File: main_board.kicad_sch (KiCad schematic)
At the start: 19 parts, among them SW1 SW_Push, SW2 SW_Push, SW3 SW_Push, U4 QM_XC7A35T_DDR3

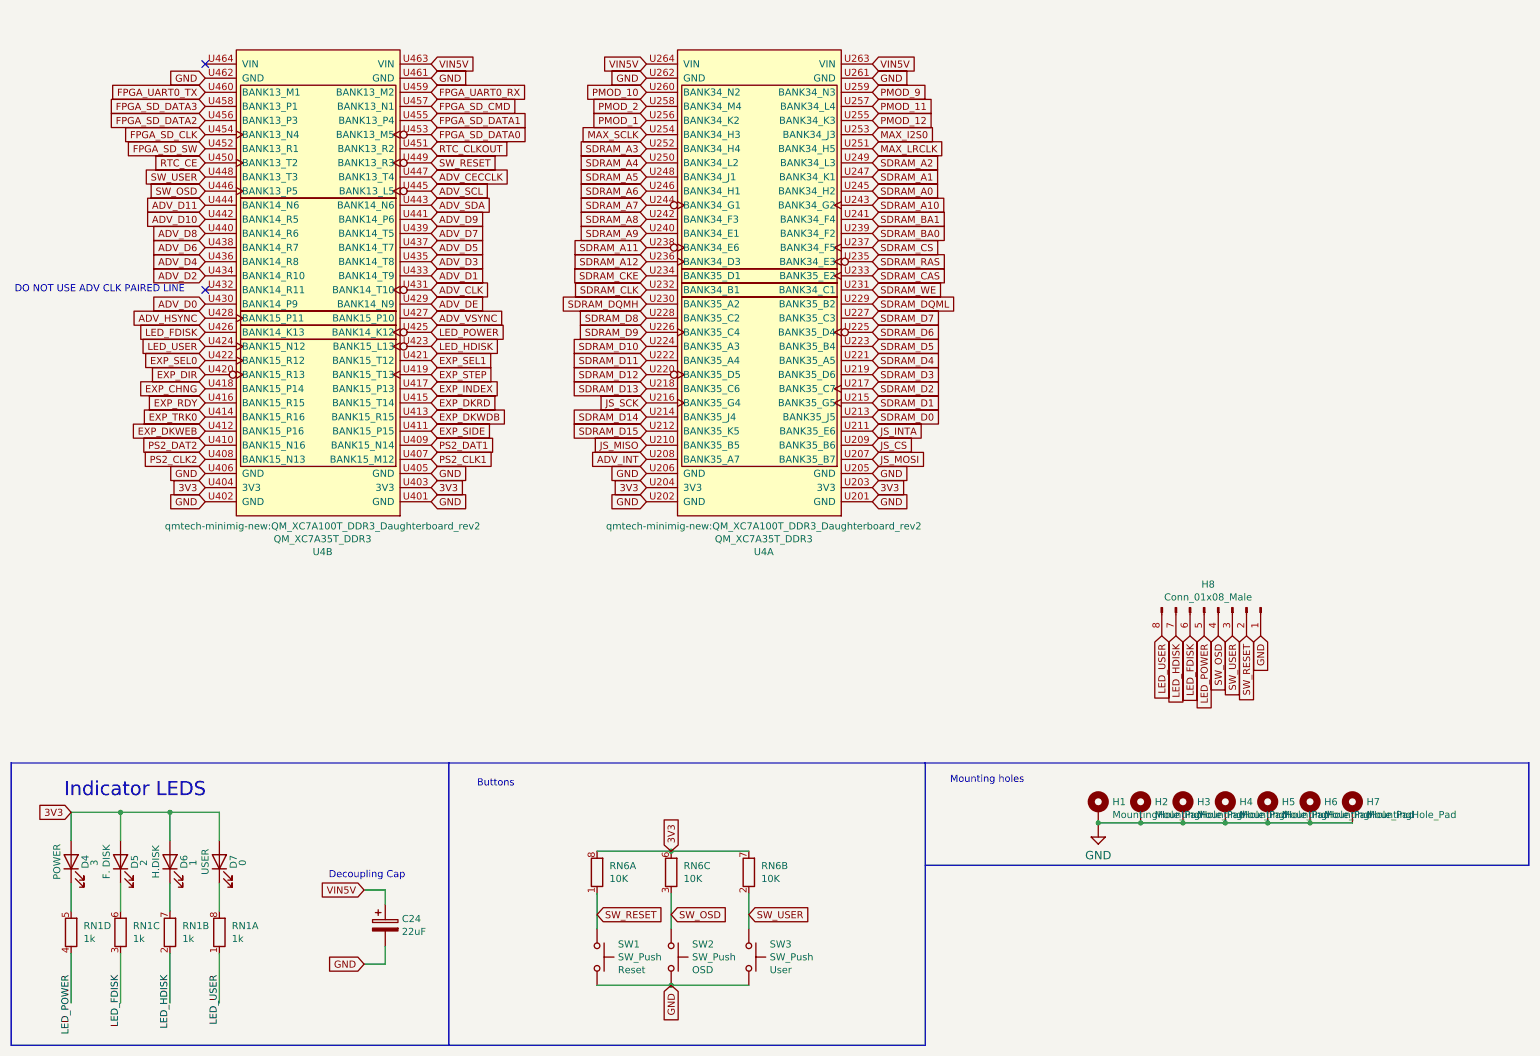
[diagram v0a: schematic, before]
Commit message: Prod version of OpenAARS 5.0 design.
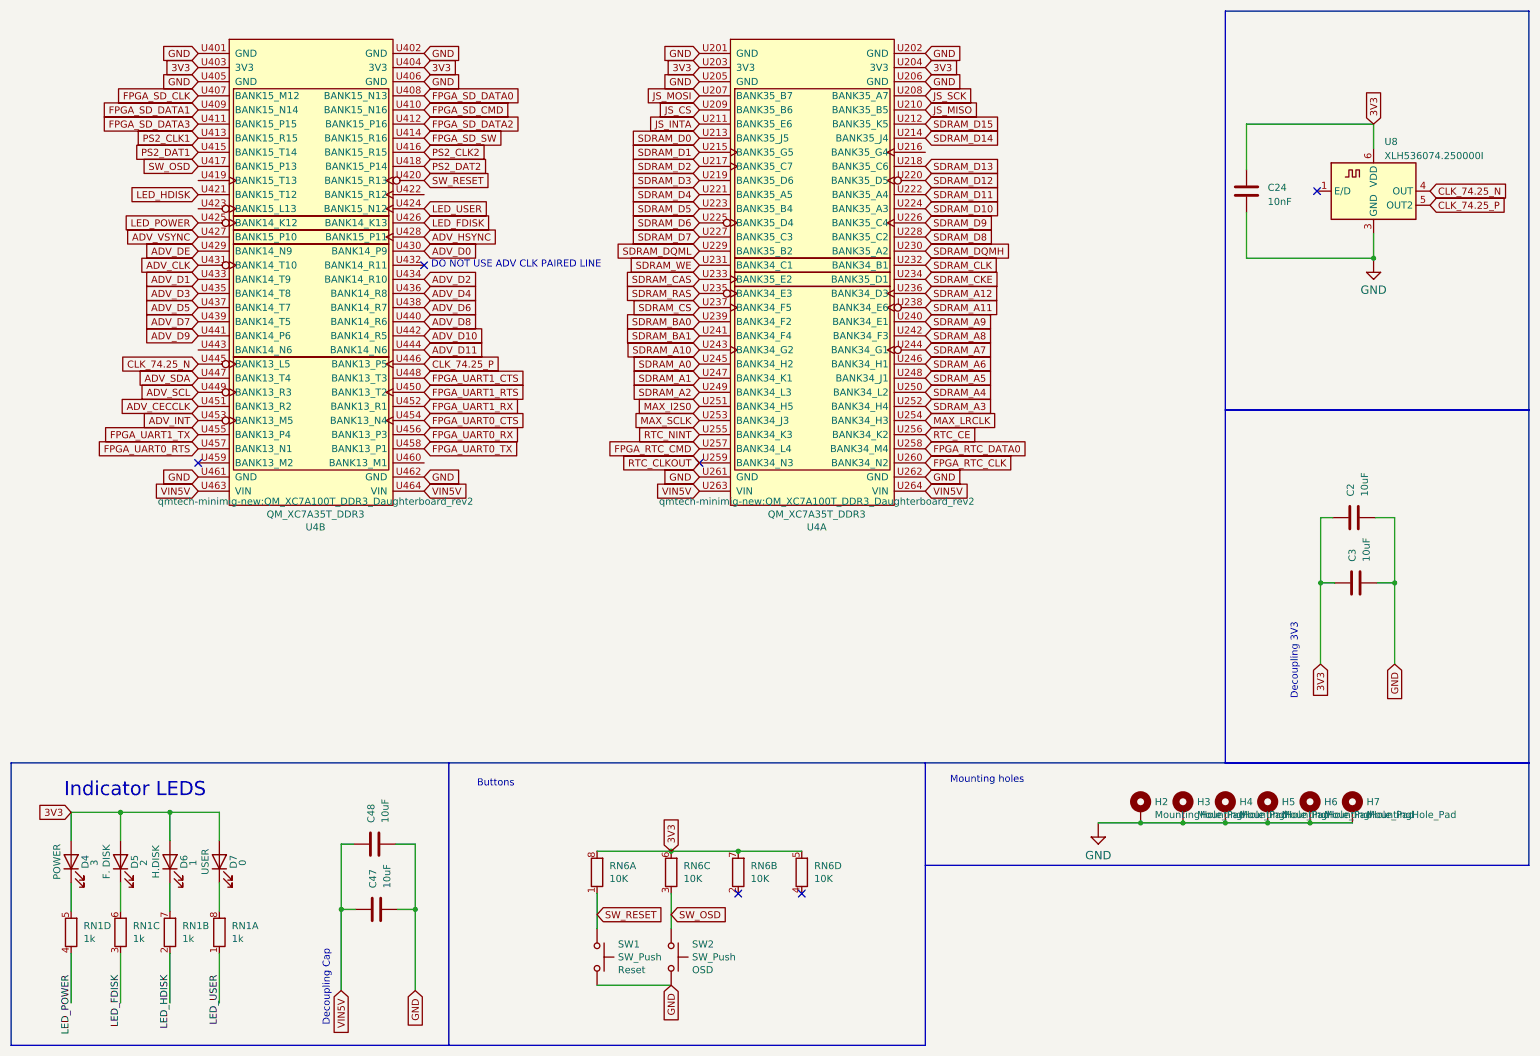
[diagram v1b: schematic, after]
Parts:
- removed C24: 22uF, Capacitor_SMD:CP_Elec_5x5.4, symbol Device:CP
- removed H1: MountingHole_Pad, MountingHole:MountingHole_3.2mm_M3_DIN965_Pad, symbol Mechanical:MountingHole_Pad
- removed H8: Conn_01x08_Male, Connector_PinHeader_2.54mm:PinHeader_1x08_P2.54mm_Vertical, symbol Connector:Conn_01x08_Male
- removed SW3: SW_Push, Button_Switch_SMD:SW_SPST_EVQQ2, symbol Switch:SW_Push
- added C2, C3, C47, C48: 10uF, Capacitor_SMD:C_1206_3216Metric, symbol Device:C
- added C24: 10nF, Capacitor_SMD:C_0603_1608Metric, symbol Device:C
- added unit 4 of RN6
- added U8: XLH536074.250000I, Oscillator:Oscillator_SMD_IDT_JS6-6_5.0x3.2mm_P1.27mm, symbol Oscillator:XUX51
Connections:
- net EXP_CHNG is gone; now on net PS2_DAT2: U4.U418 (BANK15_P14)
- net EXP_DIR is gone; now on net SW_RESET: U4.U420 (BANK15_R13)
- net EXP_DKRD is gone; now on net PS2_DAT1: U4.U415 (BANK15_T14)
- net EXP_DKWDB is gone; now on net PS2_CLK1: U4.U413 (BANK15_R15)
- net EXP_DKWEB is gone; now on net FPGA_SD_DATA2: U4.U412 (BANK15_P16)
- net EXP_INDEX is gone; now on net SW_OSD: U4.U417 (BANK15_P13)
- net EXP_RDY is gone; now on net PS2_CLK2: U4.U416 (BANK15_R15)
- net EXP_SEL1 is gone; now on net LED_HDISK: U4.U421 (BANK15_T12)
- net EXP_SIDE is gone; now on net FPGA_SD_DATA3: U4.U411 (BANK15_P15)
- net EXP_TRK0 is gone; now on net FPGA_SD_SW: U4.U414 (BANK15_R16)
- net PMOD_1 is gone; now on net RTC_CE: U4.U256 (BANK34_K2)
- net PMOD_9 is gone; now on net RTC_CLKOUT: U4.U259 (BANK34_N3)
- net 3V3: now also C2.1, C24.1, C3.1, RN6.5 (R4.2), U8.6 (VDD)
- net ADV_CECCLK: now also U4.U451 (BANK13_R2); no longer U4.U447 (BANK13_T4)
- net ADV_INT: now also U4.U453 (BANK13_M5); no longer U4.U208 (BANK35_A7)
- net ADV_SCL: now also U4.U449 (BANK13_R3); no longer U4.U445 (BANK13_L5)
- net ADV_SDA: now also U4.U447 (BANK13_T4); no longer U4.U443 (BANK14_N6)
- net FPGA_SD_CLK: now also U4.U407 (BANK15_M12); no longer U4.U454 (BANK13_N4)
- net FPGA_SD_CMD: now also U4.U410 (BANK15_N16); no longer U4.U457 (BANK13_N1)
- net FPGA_SD_DATA0: now also U4.U408 (BANK15_N13); no longer U4.U453 (BANK13_M5)
- net FPGA_SD_DATA1: now also U4.U409 (BANK15_N14); no longer U4.U455 (BANK13_P4)
- net FPGA_SD_DATA2: no longer U4.U456 (BANK13_P3)
- net FPGA_SD_DATA3: no longer U4.U458 (BANK13_P1)
- net FPGA_SD_SW: no longer U4.U452 (BANK13_R1)
- net FPGA_UART0_RX: now also U4.U456 (BANK13_P3); no longer U4.U459 (BANK13_M2)
- net FPGA_UART0_TX: now also U4.U458 (BANK13_P1); no longer U4.U460 (BANK13_M1)
- net GND: now also C2.2, C24.2, C3.2, C47.2, C48.2, U8.3 (GND)
- net JS_SCK: now also U4.U208 (BANK35_A7); no longer U4.U216 (BANK35_G4)
- net LED_HDISK: no longer U4.U423 (BANK15_L13)
- net MAX_I2S0: now also U4.U251 (BANK34_H5); no longer U4.U253 (BANK34_J3)
- net MAX_LRCLK: now also U4.U254 (BANK34_H3); no longer U4.U251 (BANK34_H5)
- net MAX_SCLK: now also U4.U253 (BANK34_J3); no longer U4.U254 (BANK34_H3)
- net PS2_CLK1: no longer U4.U407 (BANK15_M12)
- net PS2_CLK2: no longer U4.U408 (BANK15_N13)
- net PS2_DAT1: no longer U4.U409 (BANK15_N14)
- net PS2_DAT2: no longer U4.U410 (BANK15_N16)
- net RTC_CE: no longer U4.U450 (BANK13_T2)
- net RTC_CLKOUT: no longer U4.U451 (BANK13_R2)
- net SW_OSD: no longer U4.U446 (BANK13_P5)
- net SW_RESET: no longer U4.U449 (BANK13_R3)
- net VIN5V: now also U4.U464 (VIN), C47.1, C48.1
- net EXP_SEL0: no longer names the net of U4.U422 (BANK15_R12)
- net EXP_STEP: no longer names the net of U4.U419 (BANK15_T13)
- net PMOD_10 renamed FPGA_RTC_CLK
- net PMOD_11 renamed FPGA_RTC_CMD
- net PMOD_12 renamed RTC_NINT
- net PMOD_2 renamed FPGA_RTC_DATA0
- net SW_USER: no longer names the net of RN6.2 (R2.1)
- net SW_USER: no longer U4.U448 (BANK13_T3)
- new net CLK_74.25_N: U4.U445 (BANK13_L5), U8.4 (OUT)
- new net CLK_74.25_P: U4.U446 (BANK13_P5), U8.5 (OUT2)
- new net FPGA_UART0_CTS: U4.U454 (BANK13_N4)
- new net FPGA_UART0_RTS: U4.U457 (BANK13_N1)
- new net FPGA_UART1_CTS: U4.U448 (BANK13_T3)
- new net FPGA_UART1_RTS: U4.U450 (BANK13_T2)
- new net FPGA_UART1_RX: U4.U452 (BANK13_R1)
- new net FPGA_UART1_TX: U4.U455 (BANK13_P4)
- no-connect marks 2 -> 6
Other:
- note added: "Decoupling 3V3"
- moved on the sheet: U4A, U4B

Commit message: V5 Version of the board.
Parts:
- U4: value QM_XC7A35T_DDR3 -> QM_XC7A100T_DDR3; footprint qmtech-minimig-new:QM_XC7A100T_DDR3_Daughterboard_rev2 -> QM_XC7A35T_DDR3:QM_XC7A35T_DDR3_Daughterboard_v2
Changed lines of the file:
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@@
   (symbol (lib_id "QM_XC7A35T_DDR3:QM_XC7A100T_DDR3_2part") (at 156.21 57.785 0) (unit 1)
     (in_bom yes) (on_board yes) (dnp no)
-    (property "Reference" "U4" (at 156.9974 104.902 0)
-      (effects (font (size 1.27 1.27)))
-    )
-    (property "Value" "QM_XC7A35T_DDR3" (at 156.9974 102.5906 0)
-      (effects (font (size 1.27 1.27)))
-    )
-    (property "Footprint" "qmtech-minimig-new:QM_XC7A100T_DDR3_Daughterboard_rev2" (at 156.9974 100.2792 0)
+    (property "Reference" "U4" (at 156.845 107.4928 0)
+      (effects (font (size 1.27 1.27)))
+    )
+    (property "Value" "QM_XC7A100T_DDR3" (at 156.845 105.1814 0)
+      (effects (font (size 1.27 1.27)))
+    )
+    (property "Footprint" "QM_XC7A35T_DDR3:QM_XC7A35T_DDR3_Daughterboard_v2" (at 156.845 102.87 0)
       (effects (font (size 1.27 1.27)))
     )
@@
     )
   )
-  (symbol (lib_name "QM_XC7A100T_DDR3_2part_1") (lib_id "QM_XC7A35T_DDR3:QM_XC7A100T_DDR3_2part") (at 66.04 57.785 0) (unit 2)
-    (in_bom yes) (on_board yes) (dnp no)
-    (property "Reference" "U4" (at 66.8274 104.902 0)
-      (effects (font (size 1.27 1.27)))
-    )
-    (property "Value" "QM_XC7A35T_DDR3" (at 66.8274 102.5906 0)
-      (effects (font (size 1.27 1.27)))
-    )
-    (property "Footprint" "qmtech-minimig-new:QM_XC7A100T_DDR3_Daughterboard_rev2" (at 66.8274 100.2792 0)
-      (effects (font (size 1.27 1.27)))
-    )
+  (symbol (lib_id "QM_XC7A35T_DDR3:QM_XC7A100T_DDR3_2part") (at 66.04 57.785 0) (unit 2)
+    (in_bom yes) (on_board yes) (dnp no)
+    (property "Reference" "U4" (at 66.675 107.7214 0)
+      (effects (font (size 1.27 1.27)))
+    )
+    (property "Value" "QM_XC7A100T_DDR3" (at 66.675 105.41 0)
+      (effects (font (size 1.27 1.27)))
+    )
+    (property "Footprint" "QM_XC7A35T_DDR3:QM_XC7A35T_DDR3_Daughterboard_v2" (at 66.675 103.0986 0)
+      (effects (font (size 1.27 1.27)))
+    )
